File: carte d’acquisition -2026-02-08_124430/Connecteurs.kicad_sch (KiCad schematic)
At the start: 27 parts, among them J3 USB_C_Receptacle_USB2.0_14P, J4 DE9_Pins, U2 USBLC6-2SC6, U3 TCAN337G

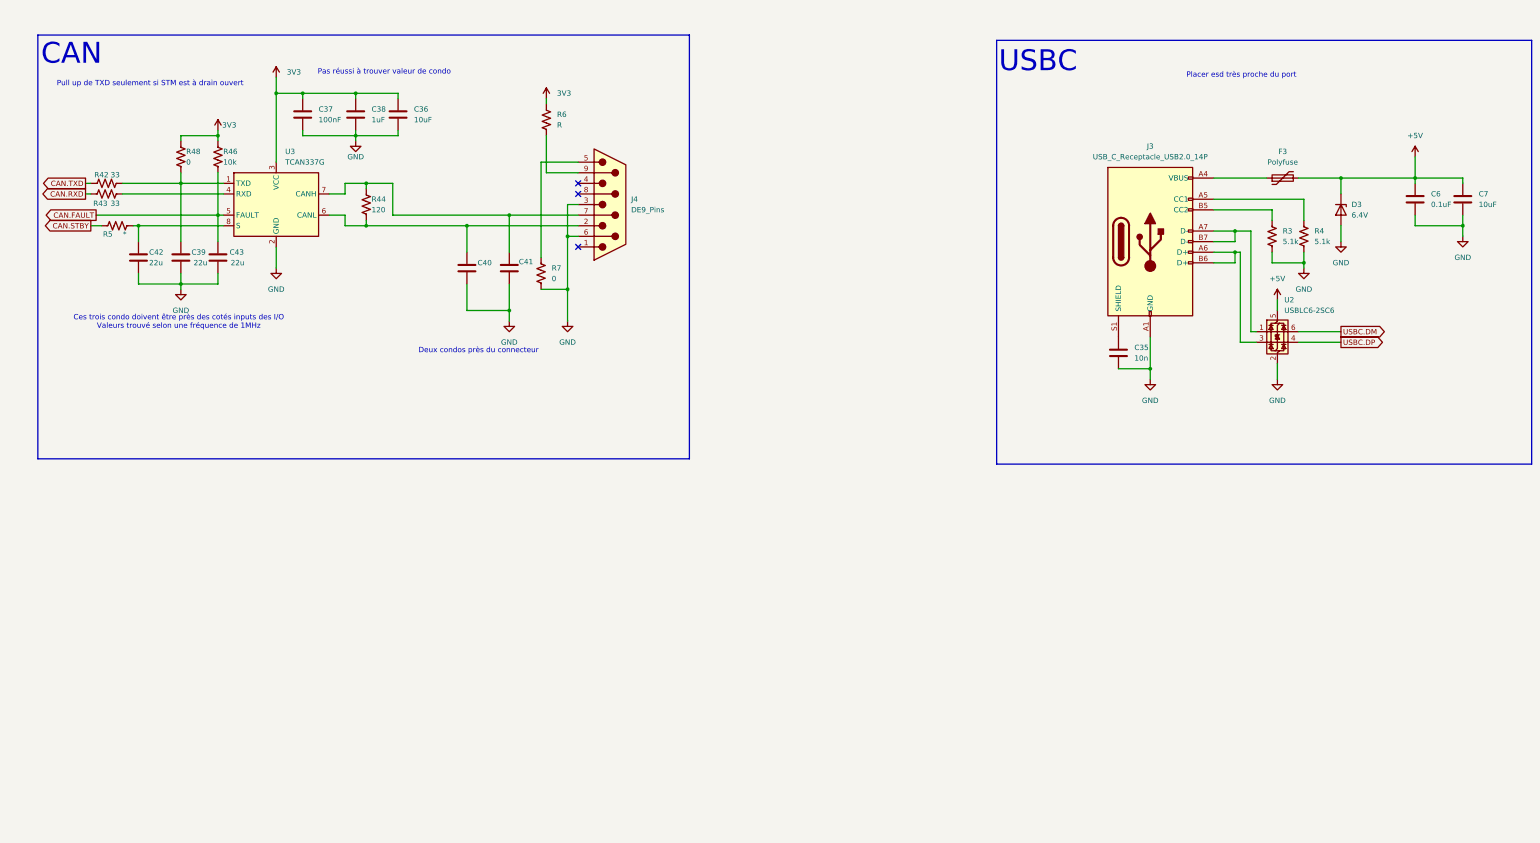
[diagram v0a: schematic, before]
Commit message: Power et maj can et sd
Modifications sur l'alim selon le schéma sur Canvas et mise à jour du can et carte sd
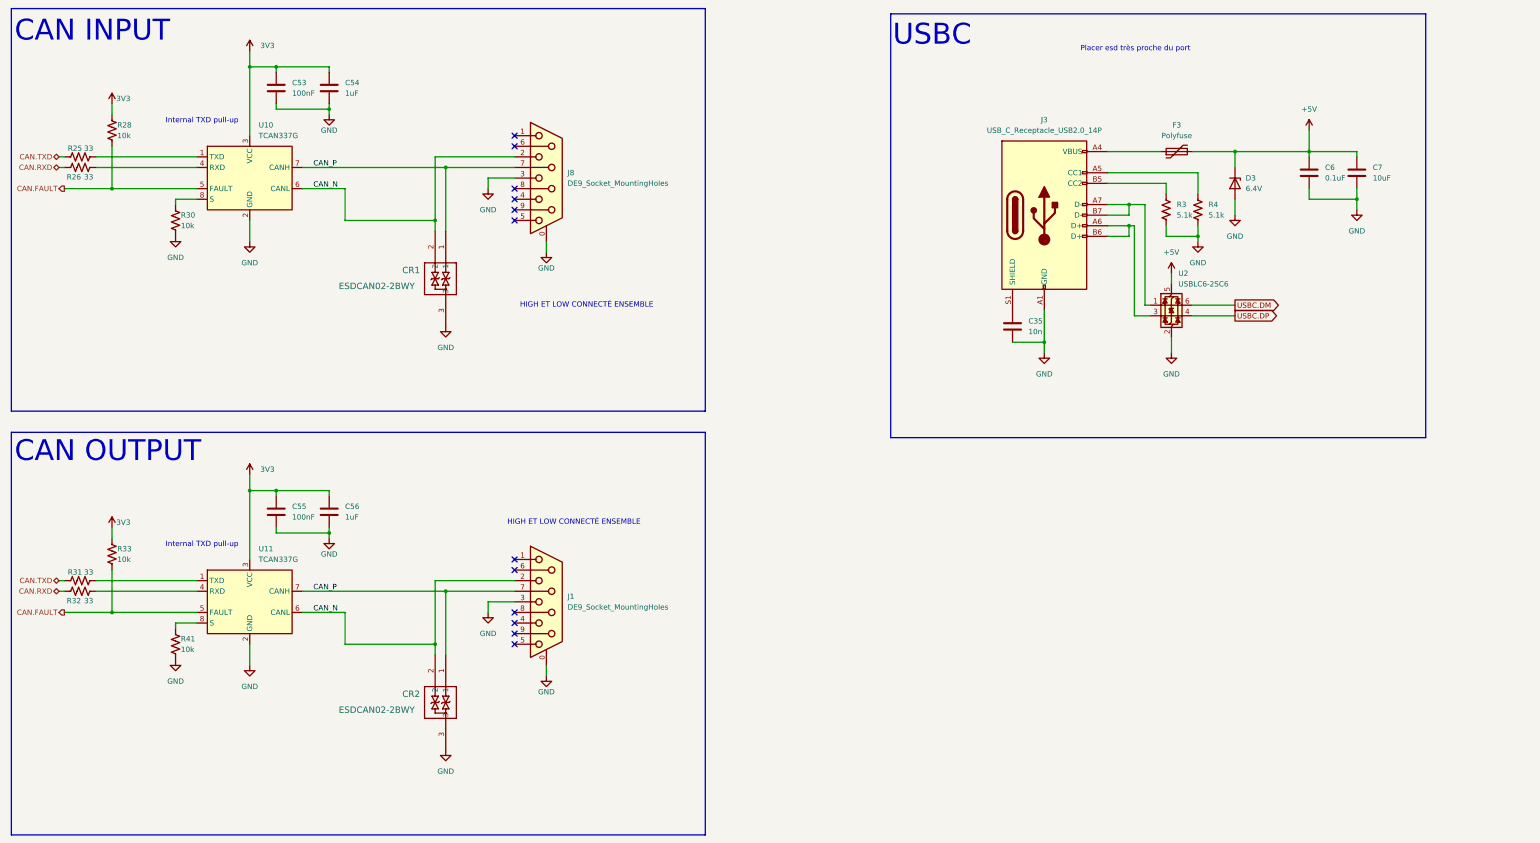
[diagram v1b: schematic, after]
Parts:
- removed C36: 10uF, symbol Device:C
- removed C37: 100nF, symbol Device:C
- removed C38: 1uF, symbol Device:C
- removed C39, C42, C43: 22u, symbol Device:C
- removed C40, C41: ~, symbol Device:C
- removed J4: DE9_Pins, symbol Connector:DE9_Pins
- removed R42, R43: 33, symbol Device:R_US
- removed R44: 120, symbol Device:R_US
- removed R46: 10k, symbol Device:R_US
- removed R48, R7: 0, symbol Device:R_US
- removed R5: *, symbol Device:R_US
- removed R6: R, symbol Device:R_US
- removed U3: TCAN337G, symbol Interface_CAN_LIN:TCAN337G
- added C53, C55: 100nF, Capacitor_SMD:C_0603_1608Metric, symbol Device:C
- added C54, C56: 1uF, Capacitor_SMD:C_0603_1608Metric, symbol Device:C
- added CR1, CR2: ESDCAN02-2BWY, symbol ESDCAN:ESDCAN02-2BWY
- added J1, J8: DE9_Socket_MountingHoles, Connector_Dsub:DSUB-9_Socket_Vertical_P2.77x2.84mm_MountingHoles, symbol Connector:DE9_Socket_MountingHoles
- added R25, R26, R31, R32: 33, Resistor_SMD:R_0603_1608Metric_Pad0.98x0.95mm_HandSolder, symbol Device:R_US
- added R28, R30, R33, R41: 10k, Resistor_SMD:R_0603_1608Metric_Pad0.98x0.95mm_HandSolder, symbol Device:R_US
- added U10, U11: TCAN337G, Package_TO_SOT_SMD:TSOT-23-8_HandSoldering, symbol Interface_CAN_LIN:TCAN337G
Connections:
- net 3V3: now also C53.1, C54.1, C55.1, C56.1, R28.1, R33.1, U10.3 (VCC), U11.3 (VCC)
- net CAN.FAULT: now also R28.2, R33.2, U10.5 (FAULT), U11.5 (FAULT)
- net CAN.RXD: now also R26.1, R32.1
- net CAN.TXD: now also R25.1, R31.1
- net GND: now also C53.2, C54.2, C55.2, C56.2, CR1.3, CR2.3, J1.0 (PAD), J1.3, J8.0 (PAD), J8.3, R30.2, R41.2, U10.2 (GND), U11.2 (GND)
- new net: R31.2, U11.1 (TXD)
- new net: R26.2, U10.4 (RXD)
- new net: R32.2, U11.4 (RXD)
- new net: R25.2, U10.1 (TXD)
- new net: R30.1, U10.8 (S)
- new net: R41.1, U11.8 (S)
- new net CAN_N: CR1.2, CR2.2, J1.2, J8.2, U10.6 (CANL), U11.6 (CANL)
- new net CAN_P: CR1.1, CR2.1, J1.7, J8.7, U10.7 (CANH), U11.7 (CANH)
- no-connect marks 3 -> 12
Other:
- note added: "CAN INPUT"
- note added: "CAN OUTPUT"
- note added: "HIGH ET LOW CONNECTÉ ENSEMBLE"
- note added: "Internal TXD pull-up"
- note removed: "CAN"
- note removed: "Ces trois condo doivent être près des cotés inputs des I/O Valeurs trouvé selon une fréquence de 1MHz"
- note removed: "Deux condos près du connecteur"
- note removed: "Pas réussi à trouver valeur de condo"
- note removed: "Pull up de TXD seulement si STM est à drain ouvert"
- moved on the sheet: C35, C6, C7, D3, F3, J3, R3, R4, U2

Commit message: Mis a jour plusieurs circuit et ajouter beaucoup de footprint manquant
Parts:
- C35, C6, C7: footprint (none) -> Capacitor_SMD:C_0603_1608Metric
- CR1, CR2: footprint (none) -> ESDCAN:SOT323-3L_STM
- D3: footprint (none) -> Diode_SMD:D_0603_1608Metric
- F3: footprint (none) -> Fuse:Fuse_0603_1608Metric
- J3: footprint (none) -> Connector_USB:USB_C_Receptacle_GCT_USB4105-xx-A_16P_TopMnt_Horizontal
- R3, R4: footprint (none) -> Resistor_SMD:R_0603_1608Metric
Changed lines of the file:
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@@
 			)
 		)
-		(property "Footprint" ""
+		(property "Footprint" "Resistor_SMD:R_0603_1608Metric"
 			(at 299.466 68.834 90)
 			(effects
@@
 			)
 		)
-		(property "Footprint" ""
+		(property "Footprint" "Capacitor_SMD:C_0603_1608Metric"
 			(at 345.1352 63.5 0)
 			(effects
@@
 			)
 		)
-		(property "Footprint" ""
+		(property "Footprint" "Fuse:Fuse_0603_1608Metric"
 			(at 306.07 53.34 0)
 			(effects
@@
 			)
 		)
-		(property "Footprint" ""
+		(property "Footprint" "Diode_SMD:D_0603_1608Metric"
 			(at 314.96 62.23 0)
 			(effects
@@
 			)
 		)
-		(property "Footprint" ""
+		(property "Footprint" "Capacitor_SMD:C_0603_1608Metric"
 			(at 333.7052 63.5 0)
 			(effects
@@
 			)
 		)
-		(property "Footprint" ""
+		(property "Footprint" "Resistor_SMD:R_0603_1608Metric"
 			(at 307.086 68.834 90)
 			(effects
@@
 			)
 		)
-		(property "Footprint" ""
+		(property "Footprint" "ESDCAN:SOT323-3L_STM"
 			(at 125.73 175.26 0)
 			(effects
@@
 			)
 		)
-		(property "Footprint" ""
+		(property "Footprint" "Capacitor_SMD:C_0603_1608Metric"
 			(at 262.5852 100.33 0)
 			(effects
@@
 			)
 		)
-		(property "Footprint" ""
+		(property "Footprint" "Connector_USB:USB_C_Receptacle_GCT_USB4105-xx-A_16P_TopMnt_Horizontal"
 			(at 273.05 69.85 0)
 			(effects
@@
 			)
 		)
-		(property "Footprint" ""
+		(property "Footprint" "ESDCAN:SOT323-3L_STM"
 			(at 125.73 73.66 0)
 			(effects
